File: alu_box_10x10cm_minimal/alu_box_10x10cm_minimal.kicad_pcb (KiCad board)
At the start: 2 copper layers, 95 x 100 mm, 8 parts

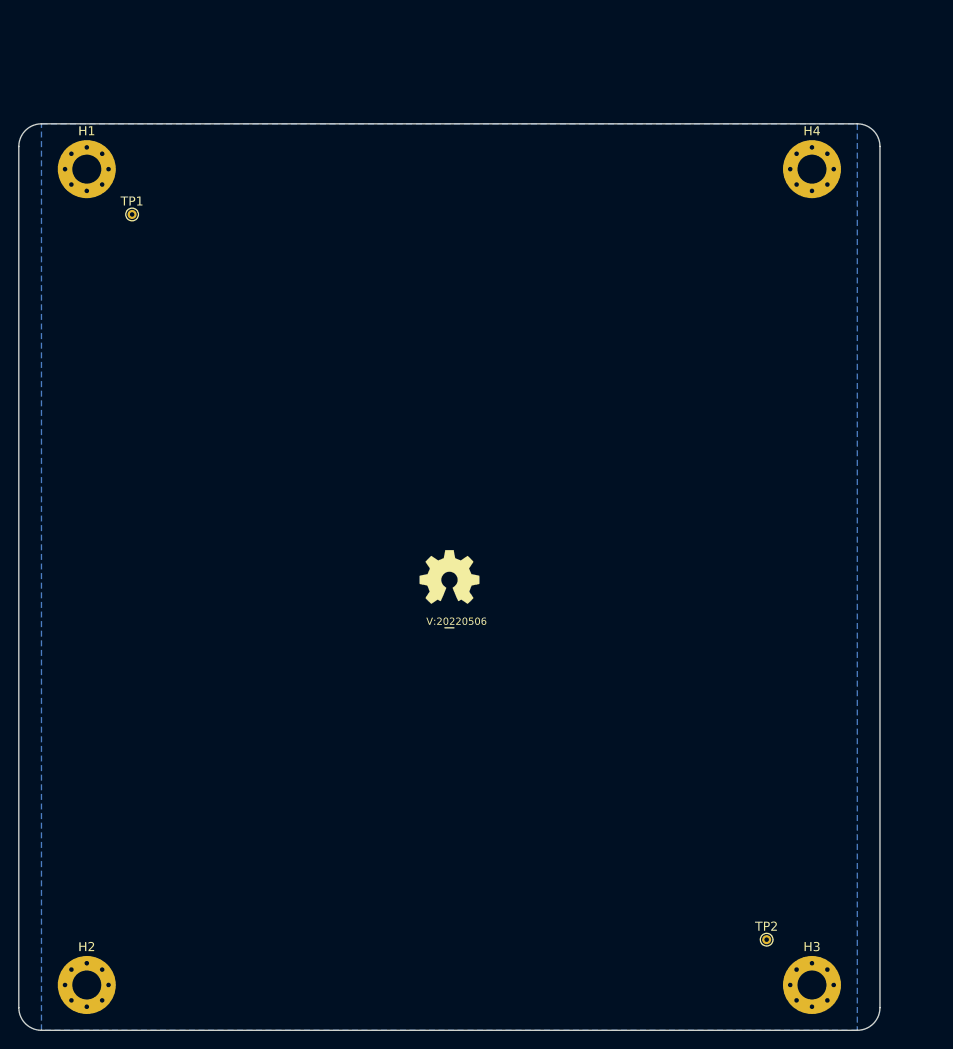
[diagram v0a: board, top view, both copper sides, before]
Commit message: updated minimal 10x10 alubox template
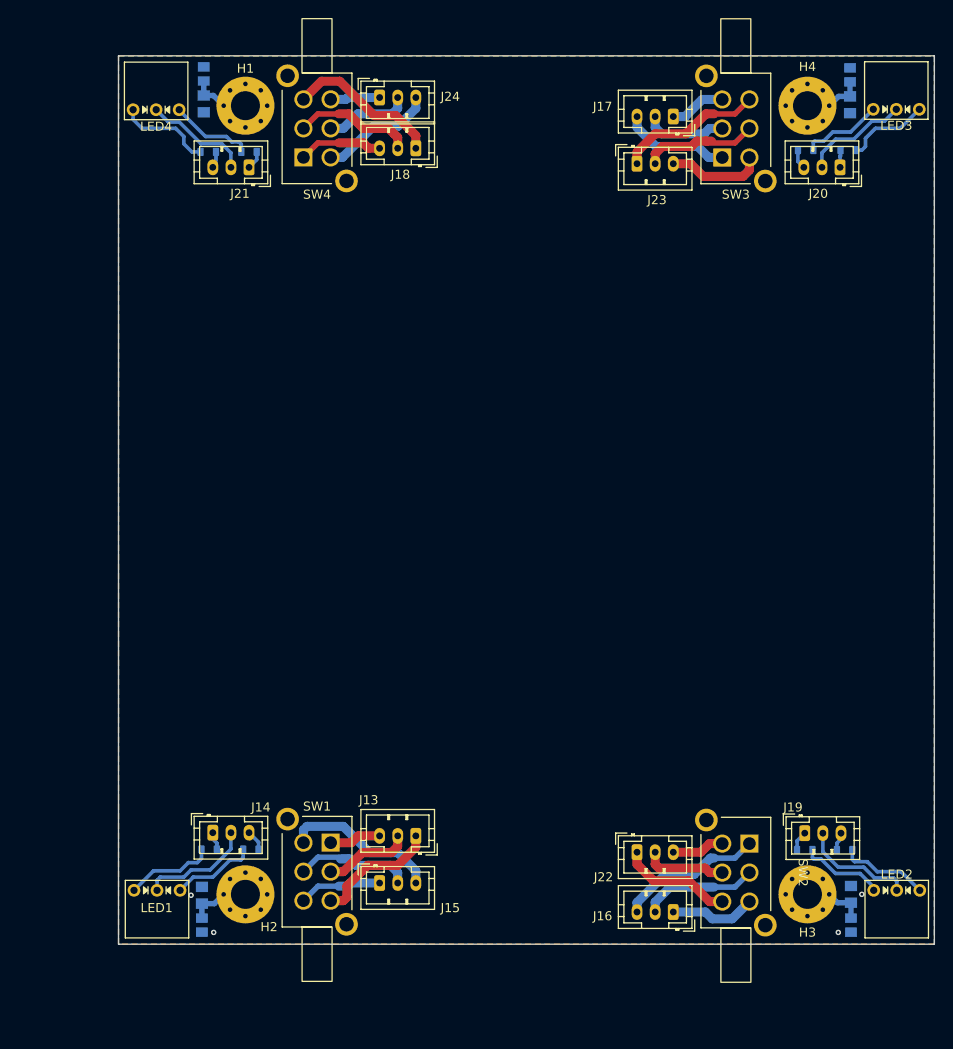
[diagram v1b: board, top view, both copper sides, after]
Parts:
- removed TP1, TP2: testpad, TestPoint:TestPoint_THTPad_D1.0mm_Drill0.5mm
- added C1: 10n, SquantorRcl:C_0805+0603, B.Cu at (122.9, 47.8)
- added C2: 10n, SquantorRcl:C_0805+0603, B.Cu at (122.7, 135.1)
- added C3: 10n, SquantorRcl:C_0805+0603, B.Cu at (194.3, 135.0)
- added C4: 10n, SquantorRcl:C_0805+0603, B.Cu at (194.2, 47.9)
- added J13: Conn_01x03, Connector_JST:JST_PH_B3B-PH-K_1x03_P2.00mm_Vertical, F.Cu at (146.3, 128.6)
- added J14: Conn_01x03, Connector_JST:JST_PH_B3B-PH-K_1x03_P2.00mm_Vertical, F.Cu at (123.9, 128.2)
- added J15: Conn_01x03, Connector_JST:JST_PH_B3B-PH-K_1x03_P2.00mm_Vertical, F.Cu at (142.3, 133.8)
- added J16: Conn_01x03, Connector_JST:JST_PH_B3B-PH-K_1x03_P2.00mm_Vertical, F.Cu at (174.7, 136.9)
- added J17: Conn_01x03, Connector_JST:JST_PH_B3B-PH-K_1x03_P2.00mm_Vertical, F.Cu at (174.7, 49.2)
- added J18: Conn_01x03, Connector_JST:JST_PH_B3B-PH-K_1x03_P2.00mm_Vertical, F.Cu at (146.3, 52.7)
- added J19: Conn_01x03, Connector_JST:JST_PH_B3B-PH-K_1x03_P2.00mm_Vertical, F.Cu at (189.2, 128.2)
- added J20: Conn_01x03, Connector_JST:JST_PH_B3B-PH-K_1x03_P2.00mm_Vertical, F.Cu at (193.1, 54.8)
- added J21: Conn_01x03, Connector_JST:JST_PH_B3B-PH-K_1x03_P2.00mm_Vertical, F.Cu at (127.9, 54.8)
- added J22: Conn_01x03, Connector_JST:JST_PH_B3B-PH-K_1x03_P2.00mm_Vertical, F.Cu at (170.7, 130.3)
- added J23: Conn_01x03, Connector_JST:JST_PH_B3B-PH-K_1x03_P2.00mm_Vertical, F.Cu at (170.7, 54.4)
- added J24: Conn_01x03, Connector_JST:JST_PH_B3B-PH-K_1x03_P2.00mm_Vertical, F.Cu at (142.3, 47.1)
- added LED1: LED_Dual_CC, SquantorDiodes:LED_DUAL_TH245_90deg, F.Cu at (117.8, 134.6)
- added LED2: LED_Dual_CC, SquantorDiodes:LED_DUAL_TH245_90deg, F.Cu at (199.3, 134.6)
- added LED3: LED_Dual_CC, SquantorDiodes:LED_DUAL_TH245_90deg, F.Cu at (199.3, 48.4)
- added LED4: LED_Dual_CC, SquantorDiodes:LED_DUAL_TH245_90deg, F.Cu at (117.7, 48.4)
- added R1: 1K, SquantorRcl:R_0805+0603, B.Cu at (122.9, 44.5)
- added R10: R, SquantorRcl:R_0603_hand, B.Cu at (189.3, 52.9)
- added R11: R, SquantorRcl:R_0603_hand, B.Cu at (127.9, 53.1)
- added R12: R, SquantorRcl:R_0603_hand, B.Cu at (123.4, 53.1)
- added R2: 1K, SquantorRcl:R_0805+0603, B.Cu at (122.7, 138.4)
- added R3: 1K, SquantorRcl:R_0805+0603, B.Cu at (194.3, 138.4)
- added R4: 1K, SquantorRcl:R_0805+0603, B.Cu at (194.2, 44.6)
- added R5: R, SquantorRcl:R_0603_hand, B.Cu at (123.5, 130.1)
- added R6: R, SquantorRcl:R_0603_hand, B.Cu at (128.1, 130.1)
- added R7: R, SquantorRcl:R_0603_hand, B.Cu at (189.2, 130.1)
- added R8: R, SquantorRcl:R_0603_hand, B.Cu at (193.6, 130.1)
- added R9: R, SquantorRcl:R_0603_hand, B.Cu at (194.0, 52.9)
- added SW1: switch_DPDT, SquantorSwitches:PS-22F02, F.Cu at (135.4, 132.5)
- added SW2: switch_DPDT, SquantorSwitches:PS-22F02, F.Cu at (181.6, 132.6)
- added SW3: switch_DPDT, SquantorSwitches:PS-22F02, F.Cu at (181.6, 50.5)
- added SW4: switch_DPDT, SquantorSwitches:PS-22F02, F.Cu at (135.4, 50.5)
- N1: moved to B.Cu
- N2: value V:20220506 -> V:20230623; moved to B.Cu
- moved H2 20.2 mm to (127.5, 135.0)
- moved H1 18.8 mm to (127.5, 48.0)
- moved N2 13.4 mm to (159.5, 95.5), turned to 180 degrees
- moved N1 12.0 mm to (158.5, 91.5), turned to 180 degrees
- moved H3 10.0 mm to (189.5, 135.0)
- moved H4 7.02 mm to (189.5, 48.0)
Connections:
- H1 pad 1: (no net) -> Net-(C1-Pad1)
- H2 pad 1: (no net) -> Net-(C2-Pad1)
- H3 pad 1: (no net) -> Net-(C3-Pad1)
- H4 pad 1: (no net) -> Net-(C4-Pad1)
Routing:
- net Net-(J15-Pad3): track 0.00 -> 17.3 mm
- net Net-(J18-Pad1): track 0.00 -> 17.1 mm
- net Net-(J16-Pad3): track 0.00 -> 16.1 mm
- net Net-(J23-Pad1): track 0.00 -> 16.1 mm
- net Net-(J15-Pad2): track 0.00 -> 13.9 mm
- net Net-(J13-Pad1): track 0.00 -> 13.8 mm
- net Net-(J23-Pad2): track 0.00 -> 13.4 mm
- net Net-(J18-Pad2): track 0.00 -> 13.3 mm
- net Net-(J16-Pad2): track 0.00 -> 12.8 mm
- net Net-(J24-Pad3): track 0.00 -> 12.8 mm
- net Net-(J19-Pad2): track 0.00 -> 12.6 mm
- net Net-(J14-Pad2): track 0.00 -> 12.5 mm
- net Net-(J22-Pad1): track 0.00 -> 12.4 mm
- net Net-(J17-Pad3): track 0.00 -> 12.0 mm
- net Net-(J21-Pad2): track 0.00 -> 11.8 mm
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- added copper zone on B.Cu, net GND
- added copper zone on F.Cu, net GND
- removed copper zone on B.Cu, net /VSS
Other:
- board size 95 x 100 mm -> 90 x 98 mm

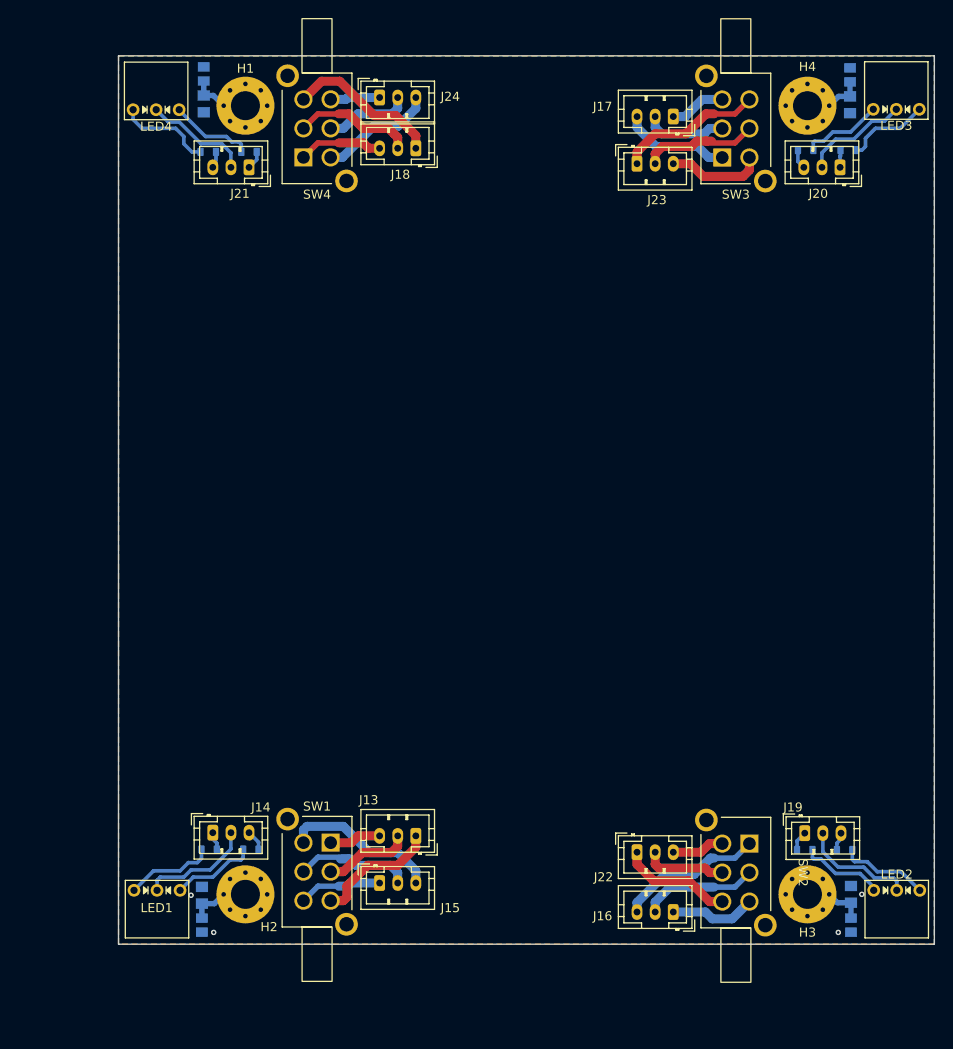
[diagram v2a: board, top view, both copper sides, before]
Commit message: adjusting mechanical dimensions to be more in line with ModEleSys V2.0
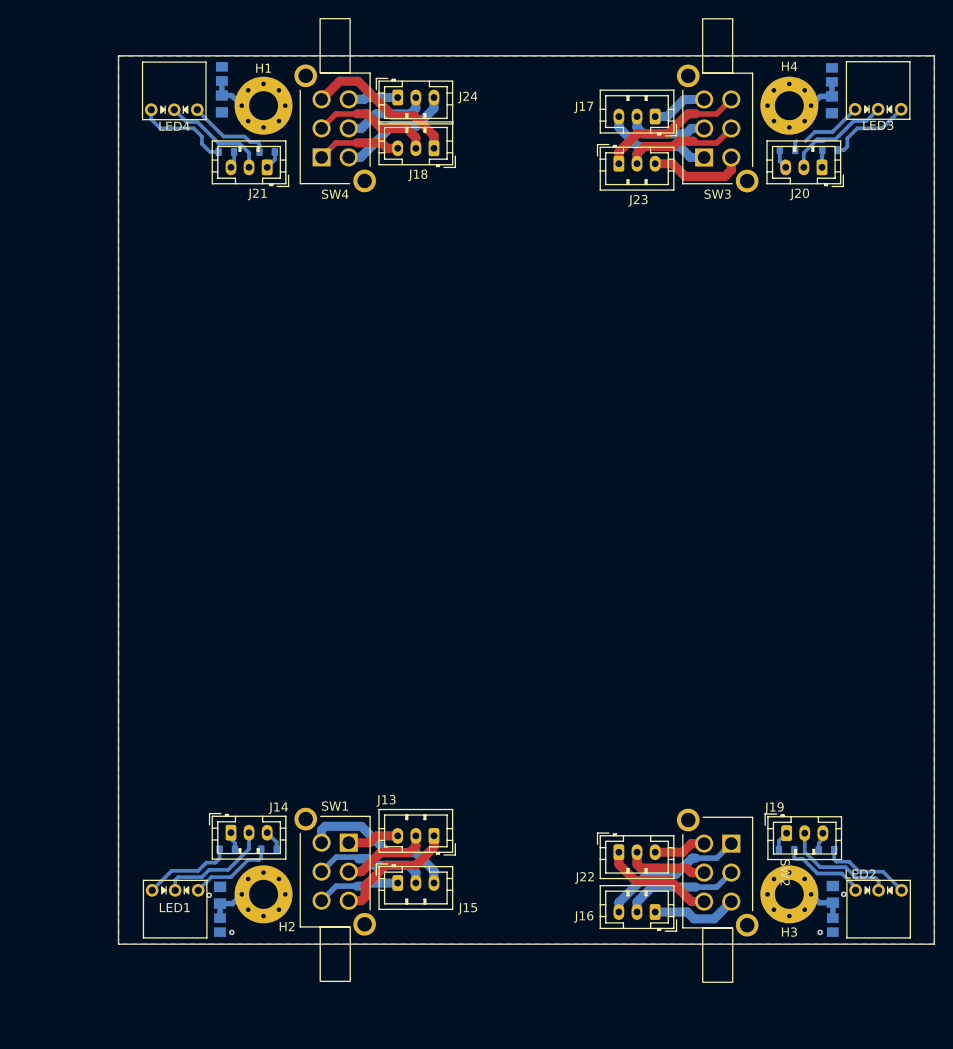
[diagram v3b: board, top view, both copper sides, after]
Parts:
- moved C1 2.00 mm to (124.9, 47.8)
- moved C2 2.00 mm to (124.7, 135.1)
- moved C3 2.00 mm to (192.3, 135.0)
- moved C4 2.00 mm to (192.2, 47.9)
- moved H1 2.00 mm to (129.5, 48.0)
- moved H2 2.00 mm to (129.5, 135.0)
- moved H3 2.00 mm to (187.5, 135.0)
- moved H4 2.00 mm to (187.5, 48.0)
- moved J13 2.00 mm to (148.3, 128.6)
- moved J14 2.00 mm to (125.9, 128.2)
- moved J15 2.00 mm to (144.3, 133.8)
- moved J16 2.00 mm to (172.7, 136.9)
- moved J17 2.00 mm to (172.7, 49.2)
- moved J18 2.00 mm to (148.3, 52.7)
- moved J19 2.00 mm to (187.2, 128.2)
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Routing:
- net Net-(LED3-Pad3): track 8.97 -> 7.97 mm
- net Net-(J20-Pad2): track 11.8 -> 12.8 mm

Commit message: updated ERC/DRC rules to match aisler
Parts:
- H1, H2, H3, H4: footprint MountingHole:MountingHole_3.2mm_M3_Pad_Via -> SquantorPcbOutline:MountingHole_3.2mm_M3_Pad_Via
- N1: footprint Symbols:OSHW-Symbol_6.7x6mm_SilkScreen -> Symbol:OSHW-Symbol_6.7x6mm_SilkScreen
- N2: value V:20230623 -> V:20240102
- moved J24 1.00 mm to (144.3, 46.1)
- moved J16 0.05 mm to (172.7, 137.0)
- moved J19 0.05 mm to (187.2, 128.2)
- moved J22 0.05 mm to (168.7, 130.4)
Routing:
- net Net-(LED3-A2): track 7.97 -> 8.97 mm
- net Net-(J24-Pin_3): track 12.8 -> 13.8 mm
- net Net-(J20-Pin_2): track 12.8 -> 11.8 mm
- net Net-(J15-Pin_2): track 13.9 -> 12.9 mm
- net Net-(J24-Pin_2): track 9.51 -> 10.5 mm
- net Net-(J23-Pin_2): track 13.4 -> 12.8 mm
- net GND: vias 4 -> 8
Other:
- rule pad_to_mask_clearance: 0.2 -> 0
